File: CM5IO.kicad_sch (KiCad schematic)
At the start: 12 parts, among them J11 USB_C_Receptacle_USB2.0

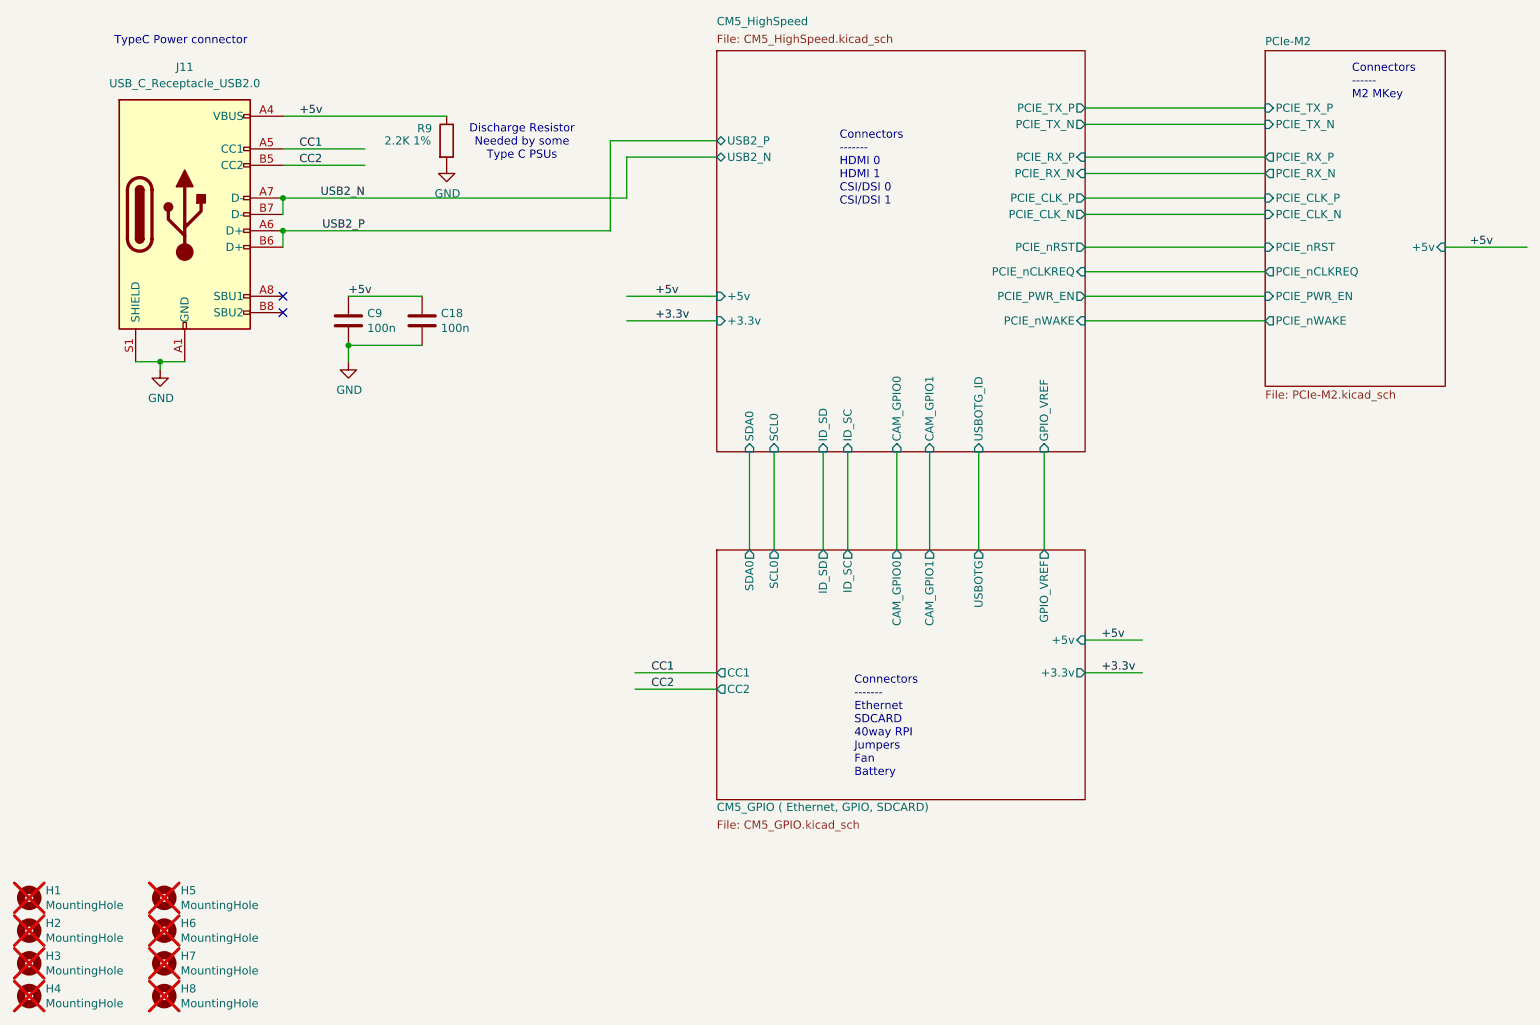
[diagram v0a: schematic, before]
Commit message: remove ethernet, pcie, hdmi
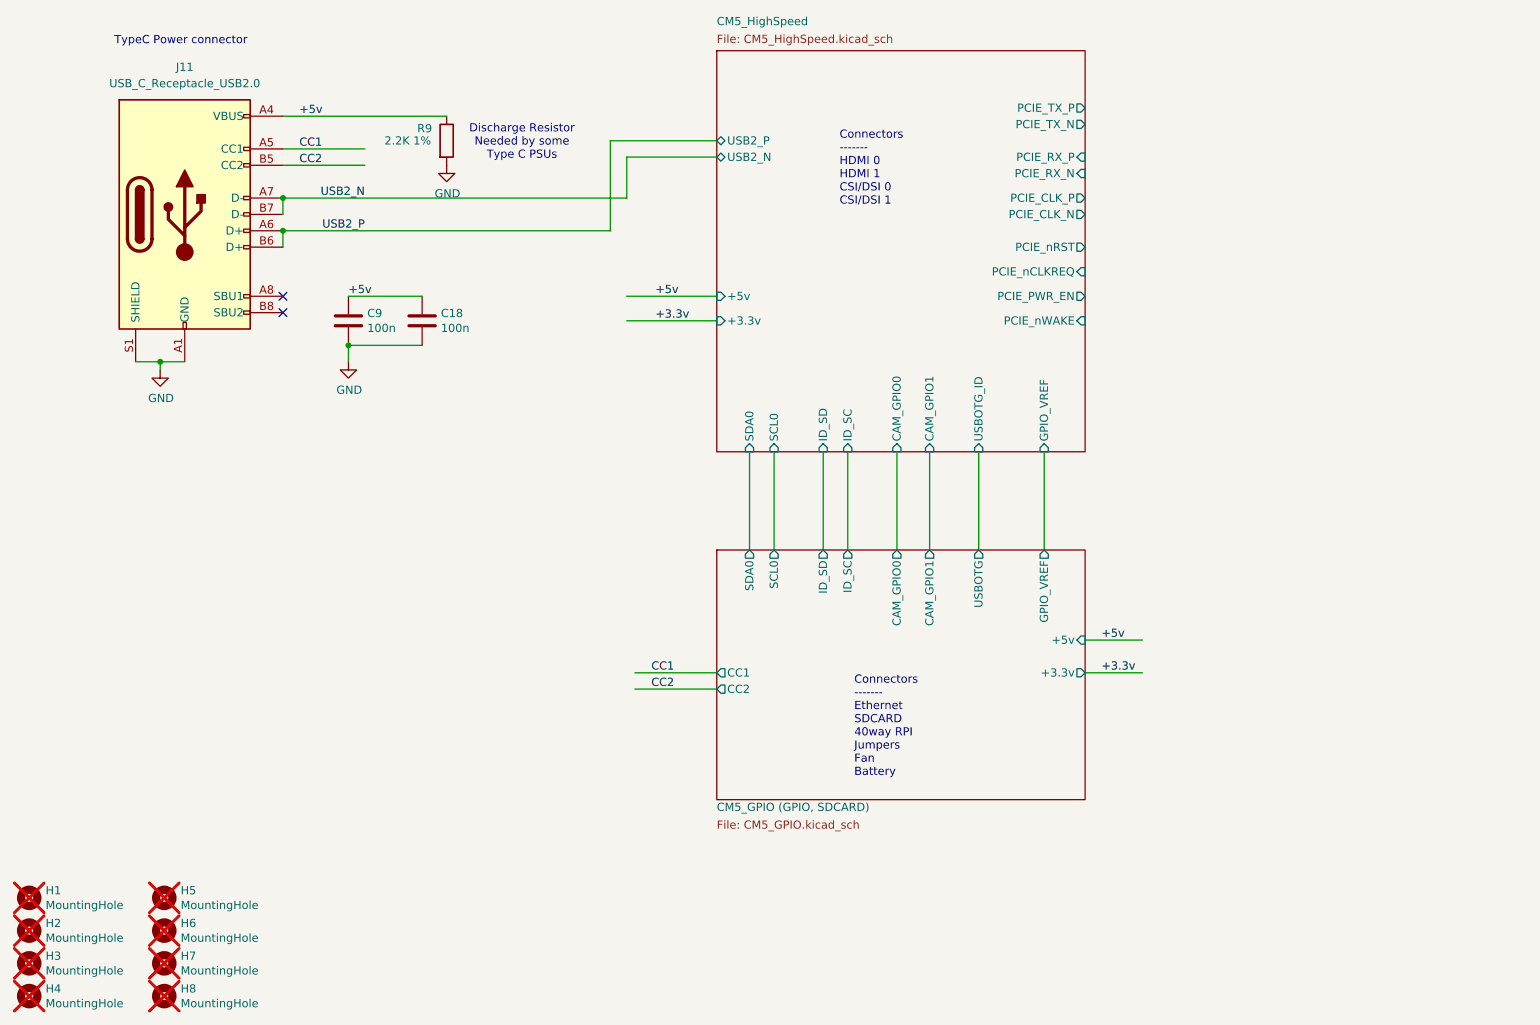
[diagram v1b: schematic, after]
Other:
- sheet CM5_GPIO ( Ethernet, GPIO, SDCARD) renamed CM5_GPIO (GPIO, SDCARD)
- removed sheet PCIe-M2
- note removed: "Connectors ------ M2 MKey"
